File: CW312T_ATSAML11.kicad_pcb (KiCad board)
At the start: 2 copper layers, 58.7 x 53.7 mm, 12 parts, among them P1 PCIEx4 EDGE CONNECTOR, U1 ATSMAL11E16A-AU

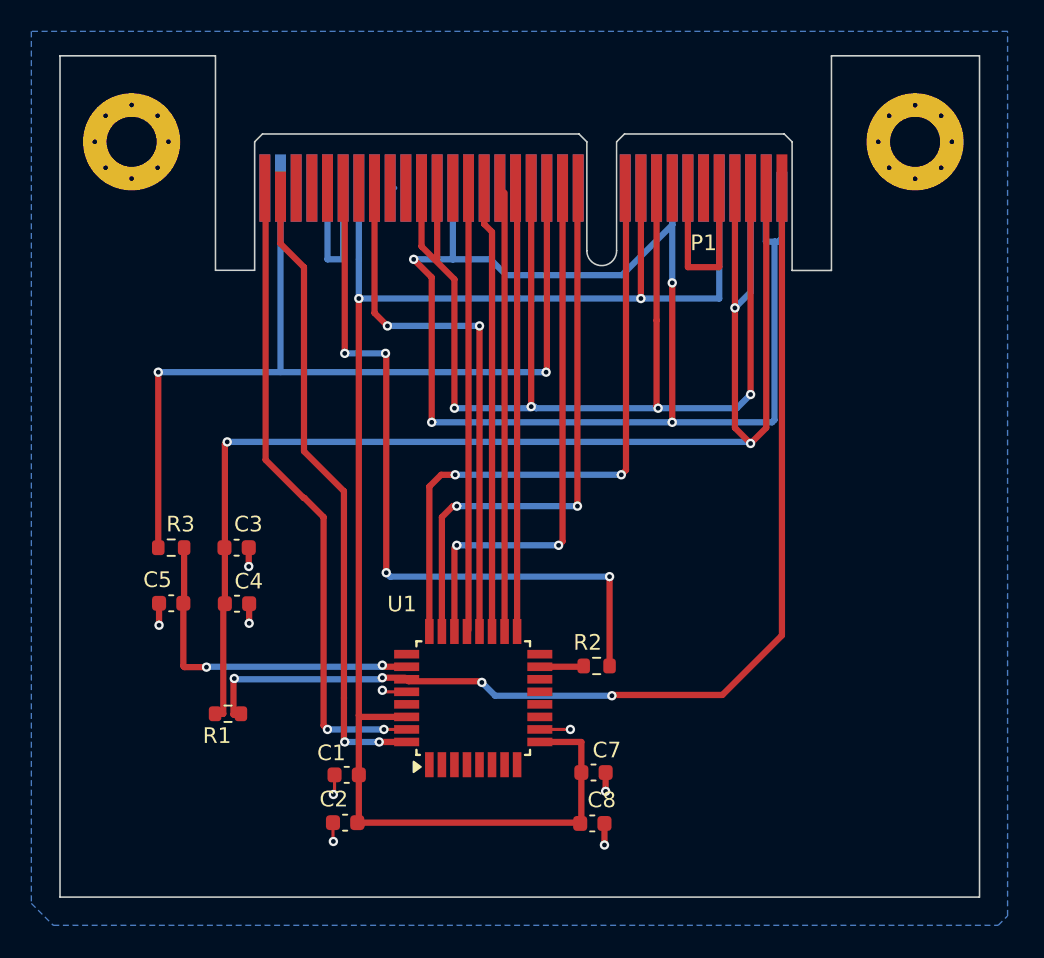
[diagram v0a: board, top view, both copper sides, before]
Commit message: updated pcb based off feedback
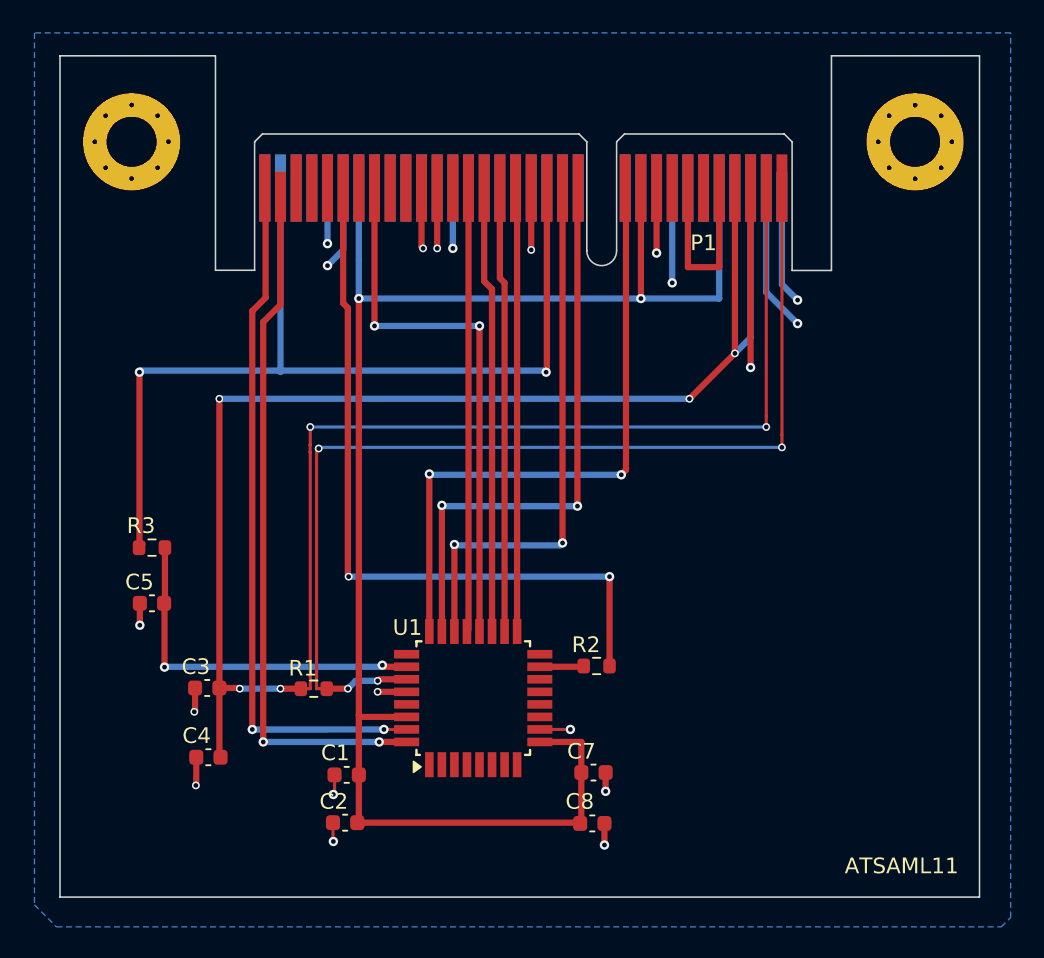
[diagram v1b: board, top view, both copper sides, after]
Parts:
- moved C4 9.97 mm to (155.6, 90.4), turned to 180 degrees
- moved C3 9.15 mm to (155.6, 86.0), turned to 180 degrees
- moved R1 5.70 mm to (162.4, 86.0)
- moved C5 1.22 mm to (152.0, 80.6)
- moved R3 1.22 mm to (152.0, 77.0)
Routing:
- net GND: track 194.1 -> 76.3 mm, vias 17 -> 20
- net /SHUNTH: track 93.1 -> 146.6 mm, vias 3 -> 7
- net /SWCLK: track 41.4 -> 49.6 mm
- net /SWDIO: track 40.4 -> 44.4 mm
- net /RST: track 59.5 -> 60.8 mm
- net Net-(U1-~{RESET}): track 22.1 -> 23.4 mm
- net /VDDCORE: track 68.4 -> 67.7 mm
- net /LED1: track 40.2 -> 40.7 mm
- net Net-(P1-CLKOUT): vias 4 -> 2
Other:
- board text added: "ATSAML11"

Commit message: updated ATSAML11 design - Ready for Review
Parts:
- added PCB1: CE, Silkscrren_Symbols:CE-Logo_8.5x6mm_SilkScreen, F.Cu at (197.8, 94.5)
- added PCB2: Pb_Free, Silkscrren_Symbols:Pb_Free_8.0x8.0mm_SilkScreen, F.Cu at (197.0, 85.7)
- added PCB3: WEEE, Silkscrren_Symbols:WEEE-Logo_5.6x8mm_SilkScreen, F.Cu at (197.1, 75.5)
- moved C6 29.2 mm to (157.7, 76.0), turned to -90 degrees
- moved C4 26.2 mm to (166.3, 66.5)
- moved C5 25.8 mm to (159.5, 76.0), turned to -90 degrees
- moved C3 20.7 mm to (166.3, 68.2)
- moved R3 19.8 mm to (171.8, 75.1), turned to 90 degrees
- moved C7 18.7 mm to (169.9, 75.1), turned to 90 degrees
- moved R1 15.7 mm to (167.0, 71.1), turned to 90 degrees
- moved R2 15.2 mm to (167.0, 91.7), turned to 0 degrees
- moved U1 7.88 mm to (165.8, 82.5), turned to 0 degrees
- moved C2 7.37 mm to (159.5, 89.0), turned to -90 degrees
- moved C1 7.10 mm to (157.8, 89.0), turned to -90 degrees
- renumbered C7 to C5, C8 to C6, C5 to C7
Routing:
- net /SHUNTH: track 146.6 -> 75.7 mm, vias 7 -> 5
- net GND: track 76.3 -> 30.9 mm, vias 20 -> 13
- net /VDDCORE: track 67.7 -> 42.9 mm, vias 4 -> 2
- net /SWCLK: track 49.6 -> 27.2 mm
- net /SWDIO: track 44.4 -> 24.8 mm, vias 2 -> 0
- net /RST: track 60.8 -> 41.7 mm, vias 2 -> 1
- net /TX: track 28.3 -> 46.6 mm, vias 0 -> 2
- net Net-(U1-~{RESET}): track 23.4 -> 5.93 mm, vias 2 -> 0
- net /RX: track 28.4 -> 45.6 mm, vias 0 -> 2
- net /GPIO3: track 28.5 -> 44.5 mm, vias 0 -> 2
- net /GPIO4: track 28.3 -> 40.9 mm, vias 0 -> 4
- net Net-(P1-CLKOUT): track 47.4 -> 55.3 mm
- net /ENTRY: track 35.0 -> 41.9 mm
- net /LED1: track 40.7 -> 37.0 mm
- net +3V3: track 103.5 -> 100.9 mm, vias 2 -> 6
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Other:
- board text added: "+1v2"
- board text added: "+3v3"
- board text added: "ATSAML11 Target Board For ChipWhisperer CW312T"
- board text added: "NewAE Technology Inc. NAE-CW312T-ATSAML11 RoHS / Pb Free"
- board text removed: "ATSAML11"

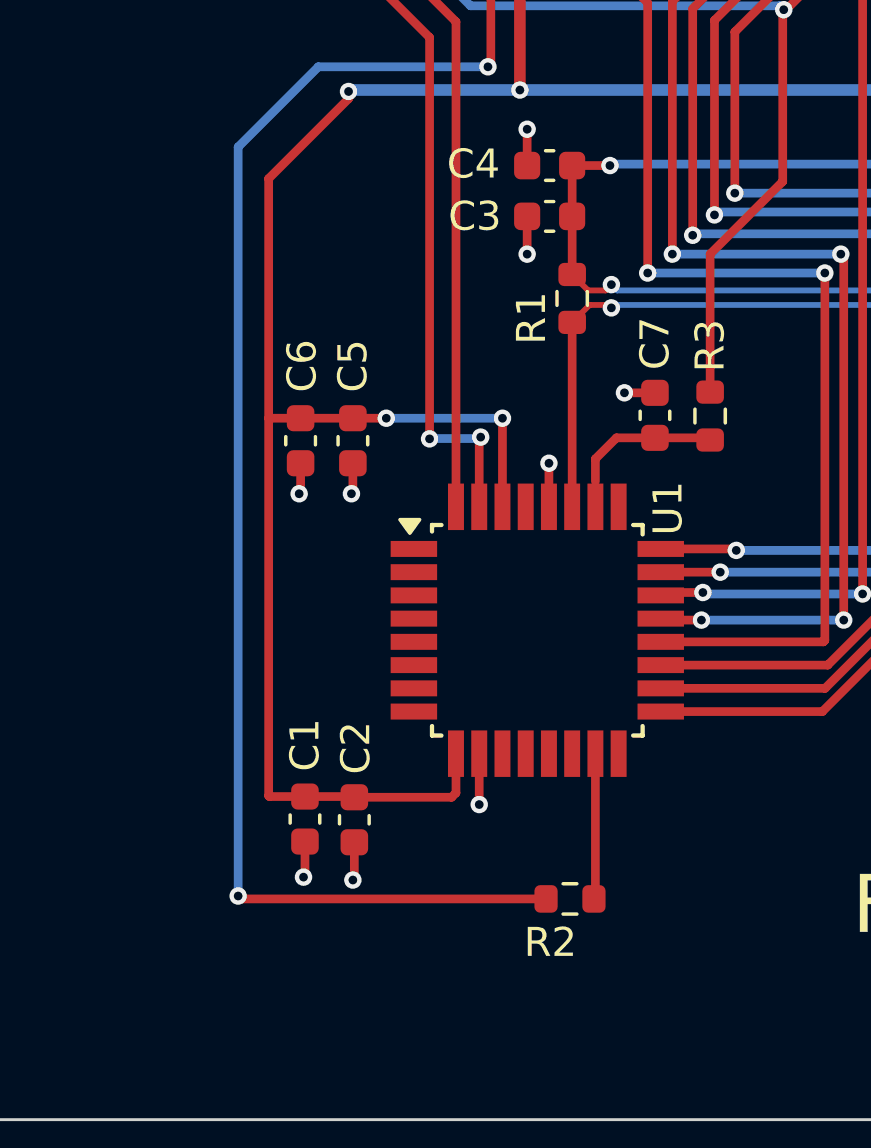
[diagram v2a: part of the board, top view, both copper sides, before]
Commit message: updated design -removed pin numbers from passives, updated cap placement, updated silkscreen
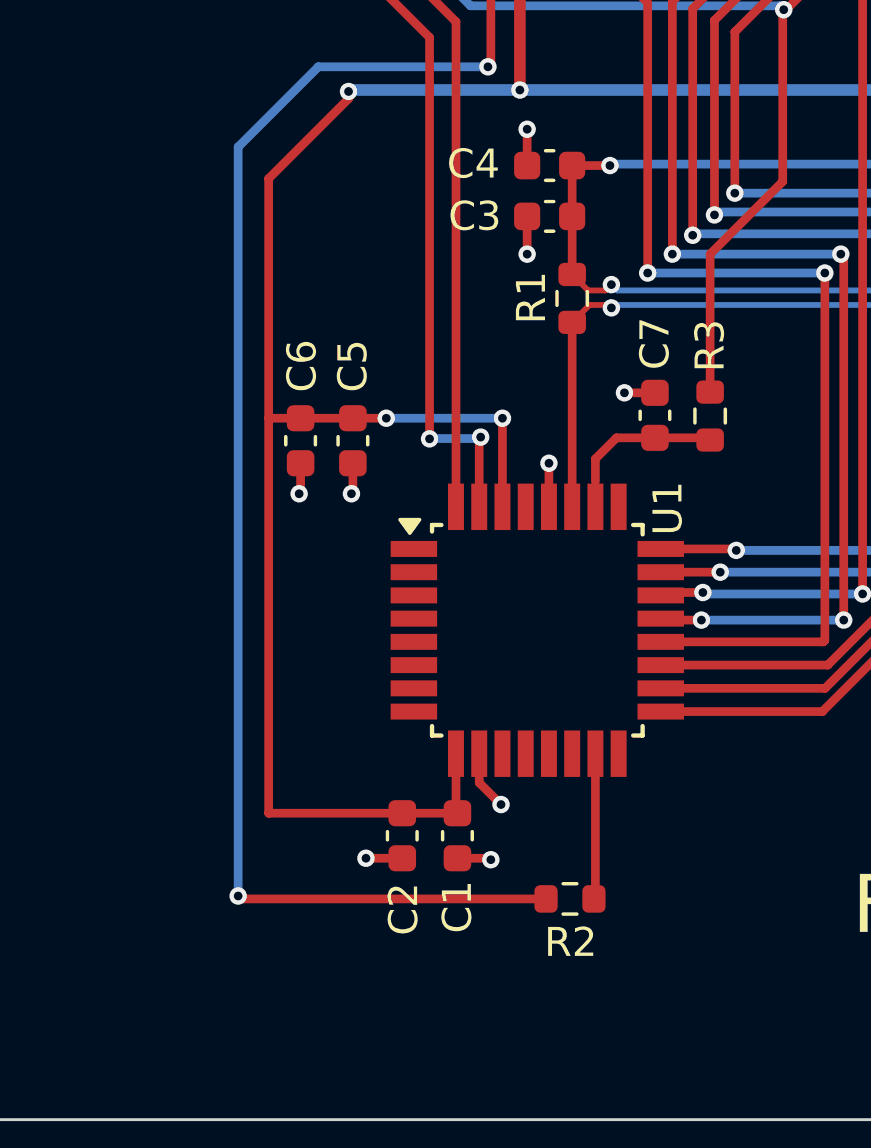
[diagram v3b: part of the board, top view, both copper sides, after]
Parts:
- added PCB4: UKCA symbol, Silkscrren_Symbols:UKCA-Logo_8x8mm_SilkScreen, F.Cu at (185.7, 94.2)
- moved PCB3 15.1 mm to (185.4, 85.1)
- moved C1 5.28 mm to (163.1, 89.6)
- moved C2 1.74 mm to (161.2, 89.6)
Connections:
- C1 pad 1: +3V3 -> (no net)
- C1 pad 2: GND -> (no net)
- C2 pad 1: +3V3 -> (no net)
- C2 pad 2: GND -> (no net)
- C3 pad 1: /SHUNTH -> (no net)
- C3 pad 2: GND -> (no net)
- C4 pad 1: /SHUNTH -> (no net)
- C4 pad 2: GND -> (no net)
- C5 pad 1: +3V3 -> (no net)
- C5 pad 2: GND -> (no net)
- C6 pad 1: +3V3 -> (no net)
- C6 pad 2: GND -> (no net)
- C7 pad 1: Net-(U1-~{RESET}) -> (no net)
- C7 pad 2: GND -> (no net)
- R1 pad 1: /VDDCORE -> (no net)
- R1 pad 2: /SHUNTH -> (no net)
- R2 pad 1: Net-(P1-CLKOUT) -> (no net)
- R2 pad 2: /XIN -> (no net)
- R3 pad 1: Net-(U1-~{RESET}) -> (no net)
- R3 pad 2: /RST -> (no net)
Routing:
- net +3V3: track 100.9 -> 102.0 mm

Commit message: Changed how pins were hidden to ensure the nets remain
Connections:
- C1 pad 1: (no net) -> +3V3
- C1 pad 2: (no net) -> GND
- C2 pad 1: (no net) -> +3V3
- C2 pad 2: (no net) -> GND
- C3 pad 1: (no net) -> /SHUNTH
- C3 pad 2: (no net) -> GND
- C4 pad 1: (no net) -> /SHUNTH
- C4 pad 2: (no net) -> GND
- C5 pad 1: (no net) -> +3V3
- C5 pad 2: (no net) -> GND
- C6 pad 1: (no net) -> +3V3
- C6 pad 2: (no net) -> GND
- C7 pad 1: (no net) -> Net-(U1-~{RESET})
- C7 pad 2: (no net) -> GND
- R1 pad 1: (no net) -> /VDDCORE
- R1 pad 2: (no net) -> /SHUNTH
- R2 pad 1: (no net) -> Net-(P1-CLKOUT)
- R2 pad 2: (no net) -> /XIN
- R3 pad 1: (no net) -> Net-(U1-~{RESET})
- R3 pad 2: (no net) -> /RST
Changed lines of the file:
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@@
 			(layers "F.Cu" "F.Paste" "F.Mask")
 			(roundrect_rratio 0.25)
+			(net 5 "/VDDCORE")
+			(pintype "passive")
 		)
 		(pad "2" smd roundrect
@@
 			(layers "F.Cu" "F.Paste" "F.Mask")
 			(roundrect_rratio 0.25)
+			(net 3 "/SHUNTH")
+			(pintype "passive")
 		)
 		(model "${KICAD8_3DMODEL_DIR}/Resistor_SMD.3dshapes/R_0603_1608Metric.wrl"
@@
 			(layers "F.Cu" "F.Paste" "F.Mask")
 			(roundrect_rratio 0.25)
+			(net 3 "/SHUNTH")
+			(pintype "passive")
 		)
 		(pad "2" smd roundrect
@@
 			(layers "F.Cu" "F.Paste" "F.Mask")
 			(roundrect_rratio 0.25)
+			(net 1 "GND")
+			(pintype "passive")
 		)
 		(model "${KICAD8_3DMODEL_DIR}/Capacitor_SMD.3dshapes/C_0603_1608Metric.wrl"
@@
 			(layers "F.Cu" "F.Paste" "F.Mask")
 			(roundrect_rratio 0.25)
+			(net 2 "+3V3")
+			(pintype "passive")
 		)
 		(pad "2" smd roundrect
@@
 			(layers "F.Cu" "F.Paste" "F.Mask")
 			(roundrect_rratio 0.25)
+			(net 1 "GND")
+			(pintype "passive")
 		)
 		(model "${KICAD8_3DMODEL_DIR}/Capacitor_SMD.3dshapes/C_0603_1608Metric.wrl"
@@
 			(layers "F.Cu" "F.Paste" "F.Mask")
 			(roundrect_rratio 0.25)
+			(net 6 "Net-(P1-CLKOUT)")
+			(pintype "passive")
 		)
 		(pad "2" smd roundrect
@@
 			(layers "F.Cu" "F.Paste" "F.Mask")
 			(roundrect_rratio 0.25)
+			(net 7 "/XIN")
+			(pintype "passive")
 		)
 		(model "${KICAD8_3DMODEL_DIR}/Resistor_SMD.3dshapes/R_0603_1608Metric.wrl"
@@
 			(layers "F.Cu" "F.Paste" "F.Mask")
 			(roundrect_rratio 0.25)
+			(net 2 "+3V3")
+			(pintype "passive")
 		)
 		(pad "2" smd roundrect
@@
 			(layers "F.Cu" "F.Paste" "F.Mask")
 			(roundrect_rratio 0.25)
+			(net 1 "GND")
+			(pintype "passive")
 		)
 		(model "${KICAD8_3DMODEL_DIR}/Capacitor_SMD.3dshapes/C_0603_1608Metric.wrl"
@@
 			(layers "F.Cu" "F.Paste" "F.Mask")
 			(roundrect_rratio 0.25)
+			(net 4 "Net-(U1-~{RESET})")
+			(pintype "passive")
 		)
 		(pad "2" smd roundrect
@@
 			(layers "F.Cu" "F.Paste" "F.Mask")
 			(roundrect_rratio 0.25)
+			(net 1 "GND")
+			(pintype "passive")
 		)
 		(model "${KICAD8_3DMODEL_DIR}/Capacitor_SMD.3dshapes/C_0603_1608Metric.wrl"
@@
 			(layers "F.Cu" "F.Paste" "F.Mask")
 			(roundrect_rratio 0.25)
+			(net 3 "/SHUNTH")
+			(pintype "passive")
 		)
 		(pad "2" smd roundrect
@@
 			(layers "F.Cu" "F.Paste" "F.Mask")
 			(roundrect_rratio 0.25)
+			(net 1 "GND")
+			(pintype "passive")
 		)
 		(model "${KICAD8_3DMODEL_DIR}/Capacitor_SMD.3dshapes/C_0603_1608Metric.wrl"
@@
 			(layers "F.Cu" "F.Paste" "F.Mask")
 			(roundrect_rratio 0.25)
+			(net 2 "+3V3")
+			(pintype "passive")
 		)
 		(pad "2" smd roundrect
@@
 			(layers "F.Cu" "F.Paste" "F.Mask")
 			(roundrect_rratio 0.25)
+			(net 1 "GND")
+			(pintype "passive")
 		)
 		(model "${KICAD8_3DMODEL_DIR}/Capacitor_SMD.3dshapes/C_0603_1608Metric.wrl"
@@
 			(layers "F.Cu" "F.Paste" "F.Mask")
 			(roundrect_rratio 0.25)
+			(net 4 "Net-(U1-~{RESET})")
+			(pintype "passive")
 		)
 		(pad "2" smd roundrect
@@
 			(layers "F.Cu" "F.Paste" "F.Mask")
 			(roundrect_rratio 0.25)
+			(net 8 "/RST")
+			(pintype "passive")
 		)
 		(model "${KICAD8_3DMODEL_DIR}/Resistor_SMD.3dshapes/R_0603_1608Metric.wrl"
@@
 			(layers "F.Cu" "F.Paste" "F.Mask")
 			(roundrect_rratio 0.25)
+			(net 2 "+3V3")
+			(pintype "passive")
 		)
 		(pad "2" smd roundrect
@@
 			(layers "F.Cu" "F.Paste" "F.Mask")
 			(roundrect_rratio 0.25)
+			(net 1 "GND")
+			(pintype "passive")
 		)
 		(model "${KICAD8_3DMODEL_DIR}/Capacitor_SMD.3dshapes/C_0603_1608Metric.wrl"

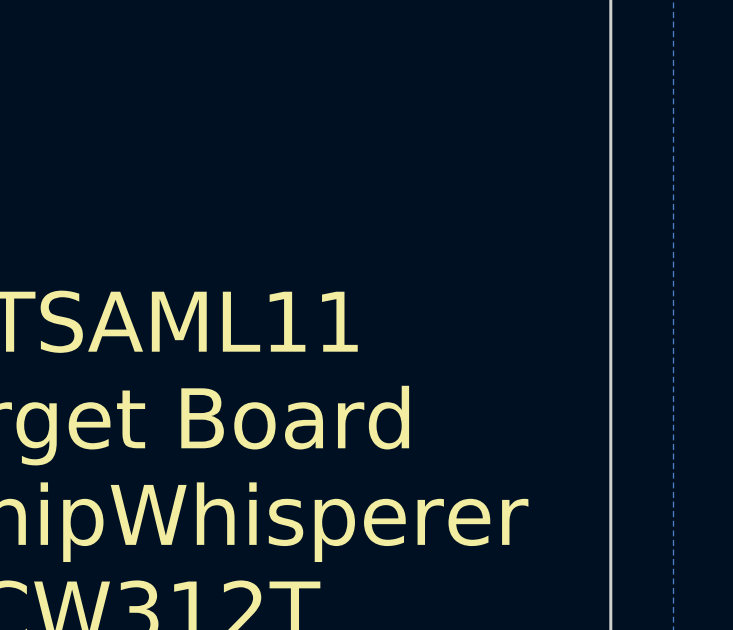
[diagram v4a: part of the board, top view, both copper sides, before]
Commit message: updated silkscreen symbols
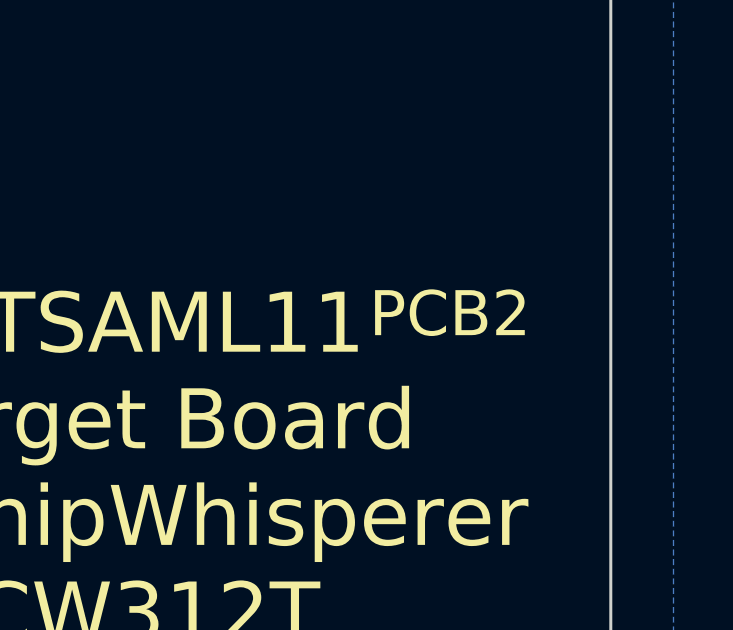
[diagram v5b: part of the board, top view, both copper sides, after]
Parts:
- PCB1: value CE -> CE Symbol
- PCB2: value Pb_Free -> Pb_Free Symbol
- PCB3: value WEEE -> UKCA symbol; footprint Silkscrren_Symbols:WEEE-Logo_5.6x8mm_SilkScreen -> Silkscrren_Symbols:UKCA-Logo_8x8mm_SilkScreen
- PCB4: value UKCA symbol -> WEEE SYMBOL; footprint Silkscrren_Symbols:UKCA-Logo_8x8mm_SilkScreen -> Silkscrren_Symbols:WEEE-Logo_5.6x8mm_SilkScreen
- moved PCB3 3.61 mm to (189.0, 85.0)
- moved PCB4 3.35 mm to (188.9, 93.3)
- moved PCB2 1.79 mm to (198.7, 85.2)
- moved PCB1 1.58 mm to (199.3, 94.0)
